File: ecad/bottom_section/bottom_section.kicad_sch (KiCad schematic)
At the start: 5 parts, among them J1 JST PH 3, J3 JST PH 3, J5 Conn_01x08

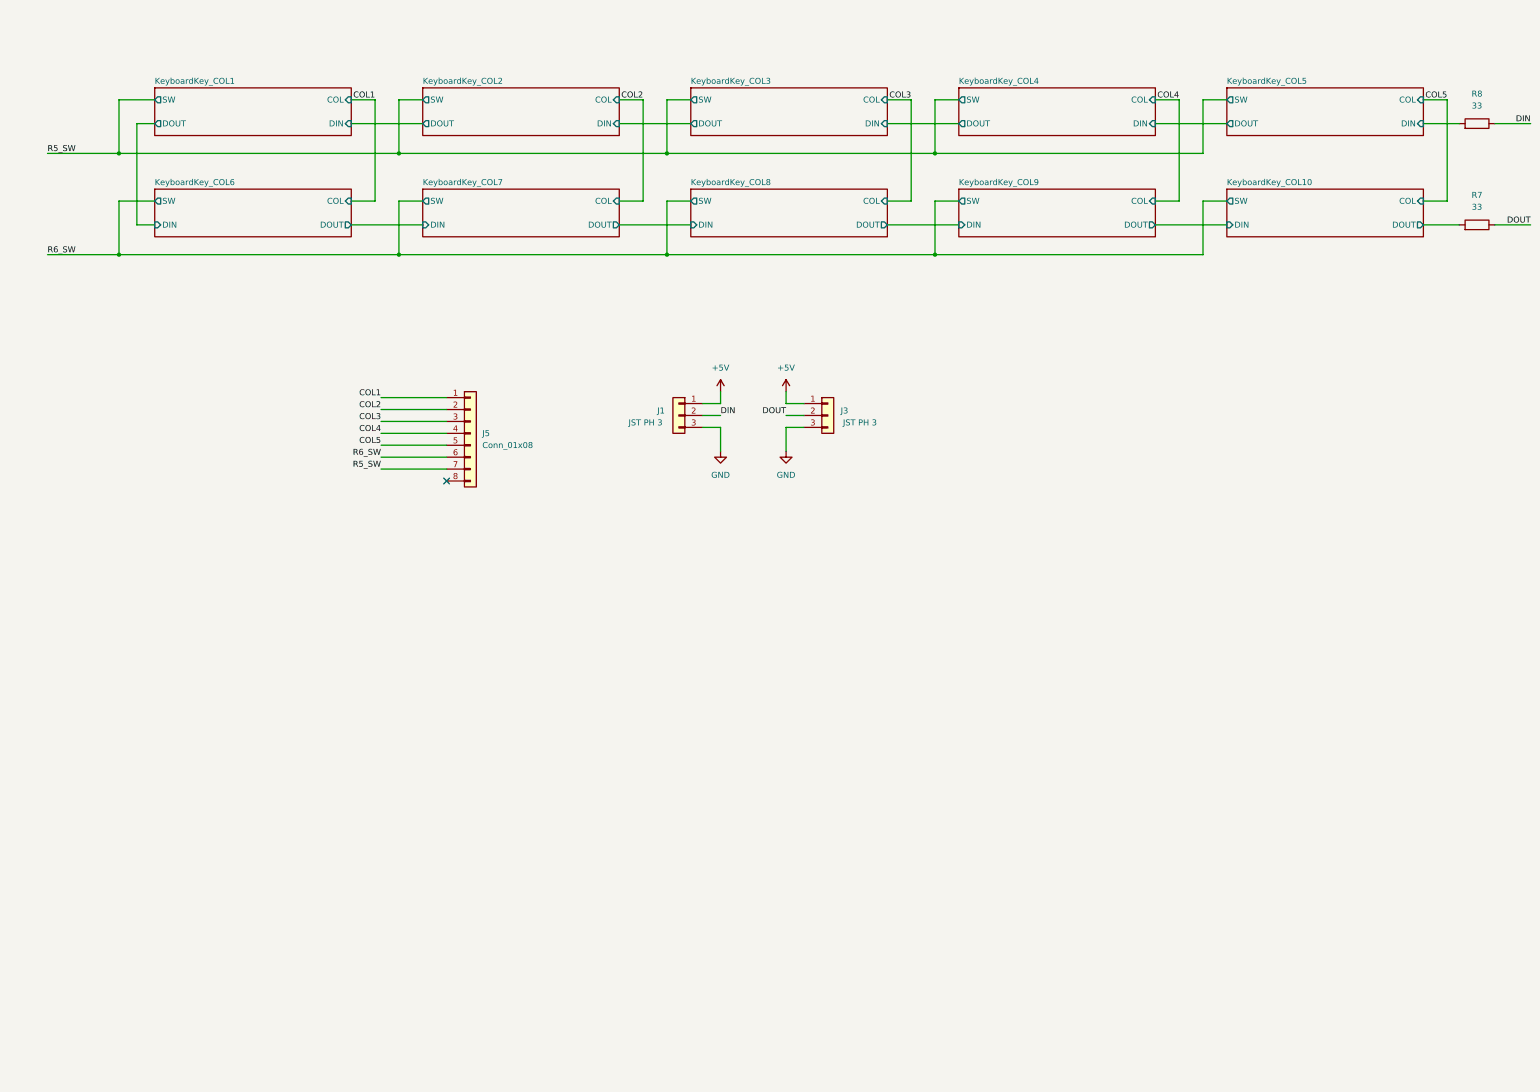
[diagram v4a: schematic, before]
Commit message: Uses LED Matrix controller on all board.
It simplifies so much the design for a small cost.
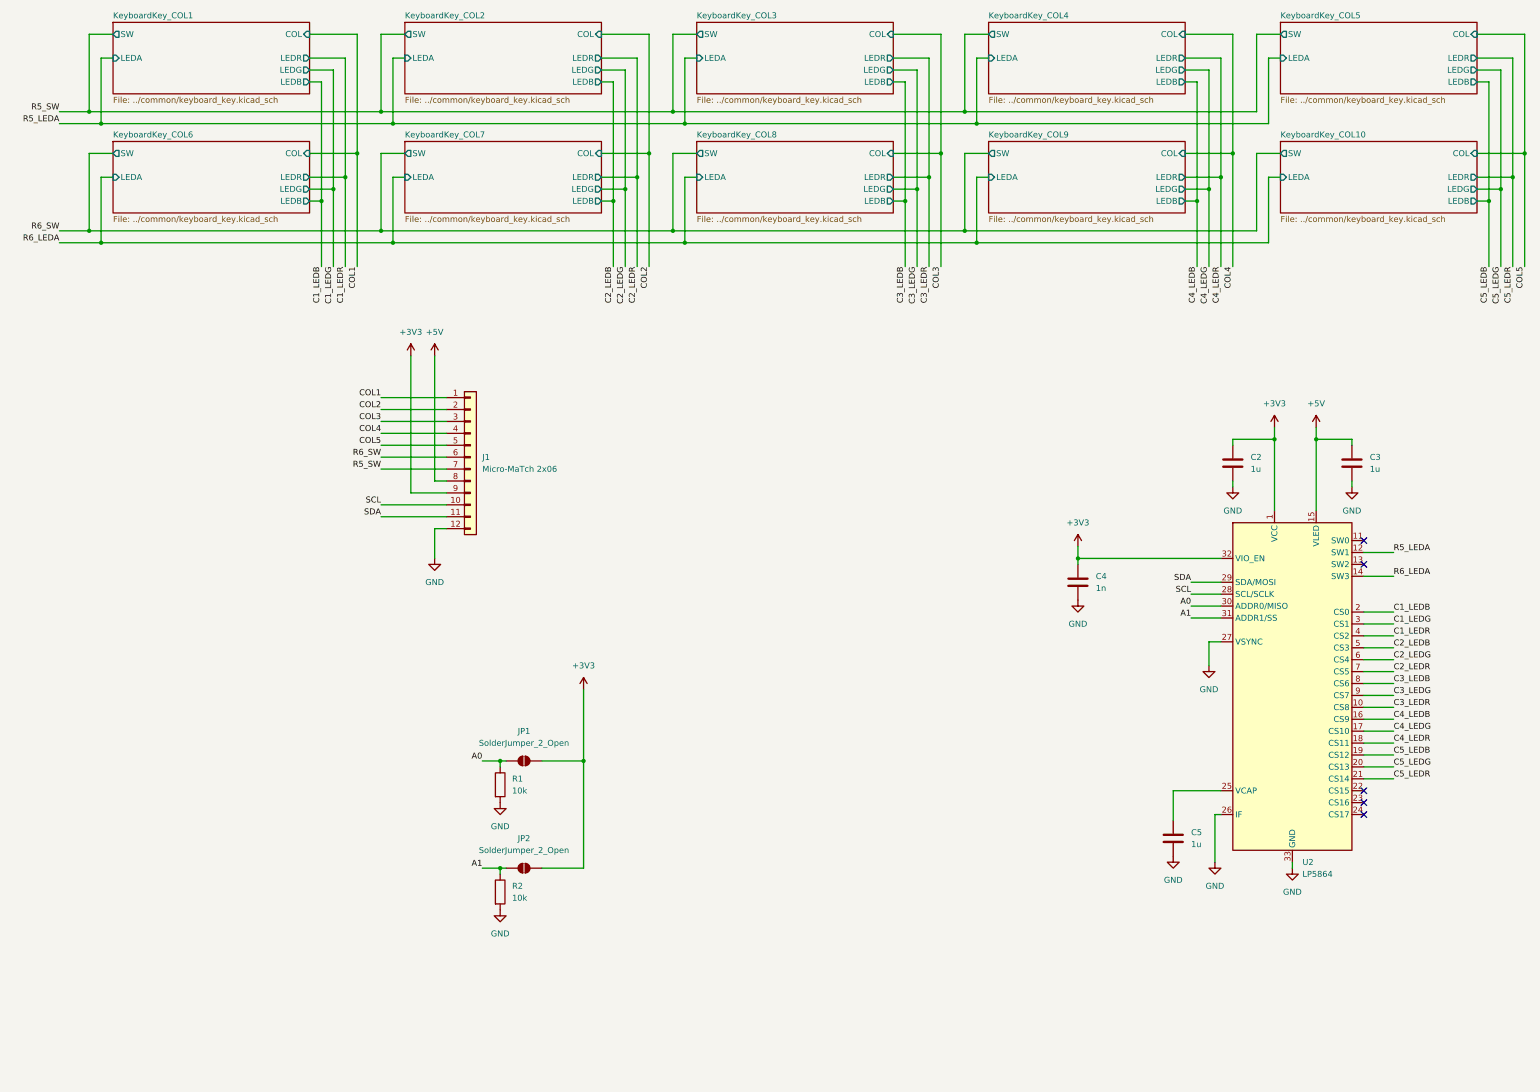
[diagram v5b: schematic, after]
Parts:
- removed J1, J3: JST PH 3, woodpecker:JST_PH_S3B-PH-SM4-TB_1x03-1MP_P2.00mm_Horizontal, symbol Connector_Generic:Conn_01x03
- removed J5: Conn_01x08, Connector_TE-Connectivity:TE_Micro-MaTch_215079-8_2x04_P1.27mm_Vertical, symbol Connector_Generic:Conn_01x08
- removed R7, R8: 33, Resistor_SMD:R_0603_1608Metric, symbol Device:R
- added C2, C3, C5: 1u, Capacitor_SMD:C_0402_1005Metric, symbol Device:C
- added C4: 1n, Capacitor_SMD:C_0402_1005Metric, symbol Device:C
- added J1: Micro-MaTch 2x06, Connector_TE-Connectivity:TE_Micro-MaTch_1-215079-2_2x06_P1.27mm_Vertical, symbol Connector_Generic:Conn_01x12
- added JP1, JP2: SolderJumper_2_Open, Jumper:SolderJumper-2_P1.3mm_Open_TrianglePad1.0x1.5mm, symbol Jumper:SolderJumper_2_Open
- added R1, R2: 10k, Resistor_SMD:R_0603_1608Metric, symbol Device:R
- added U2: LP5864, woodpecker:Texas_LP586X_VQFN-32-1EP_4x4mm_P0.4mm_EP2.8x2.8mm_ThermalVias, symbol woodpecker:LP5864
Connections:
- net +5V: now also C3.1, J1.8 (Pin_8), U2.15 (VLED)
- net COL1: now also J1.1 (Pin_1)
- net COL2: now also J1.2 (Pin_2)
- net COL3: now also J1.3 (Pin_3)
- net COL4: now also J1.4 (Pin_4)
- net COL5: now also J1.5 (Pin_5)
- net GND: now also C2.2, C3.2, C4.2, C5.2, J1.12 (Pin_12), R1.2, R2.2, U2.26 (IF), U2.27 (VSYNC), U2.33 (GND)
- net R5_SW: now also J1.7 (Pin_7)
- net R6_SW: now also J1.6 (Pin_6)
- new net: C5.1, U2.25 (VCAP)
- new net +3V3: C2.1, C4.1, J1.9 (Pin_9), JP1.2 (B), JP2.2 (B), U2.1 (VCC), U2.32 (VIO_EN)
- new net A0: JP1.1 (A), R1.1, U2.30 (ADDR0/MISO)
- new net A1: JP2.1 (A), R2.1, U2.31 (ADDR1/SS)
- new net C1_LEDB: U2.2 (CS0)
- new net C1_LEDG: U2.3 (CS1)
- new net C1_LEDR: U2.4 (CS2)
- new net C2_LEDB: U2.5 (CS3)
- new net C2_LEDG: U2.6 (CS4)
- new net C2_LEDR: U2.7 (CS5)
- new net C3_LEDB: U2.8 (CS6)
- new net C3_LEDG: U2.9 (CS7)
- new net C3_LEDR: U2.10 (CS8)
- new net C4_LEDB: U2.16 (CS9)
- new net C4_LEDG: U2.17 (CS10)
- new net C4_LEDR: U2.18 (CS11)
- new net C5_LEDB: U2.19 (CS12)
- new net C5_LEDG: U2.20 (CS13)
- new net C5_LEDR: U2.21 (CS14)
- new net R5_LEDA: U2.12 (SW1)
- new net R6_LEDA: U2.14 (SW3)
- new net SCL: J1.10 (Pin_10), U2.28 (SCL/SCLK)
- new net SDA: J1.11 (Pin_11), U2.29 (SDA/MOSI)
- no-connect marks 1 -> 5
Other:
- sheet KeyboardKey_COL1 ports: added LEDA, LEDB, LEDG, LEDR; removed DIN, DOUT
- sheet KeyboardKey_COL10 ports: added LEDA, LEDB, LEDG, LEDR; removed DIN, DOUT
- sheet KeyboardKey_COL2 ports: added LEDA, LEDB, LEDG, LEDR; removed DIN, DOUT
- sheet KeyboardKey_COL3 ports: added LEDA, LEDB, LEDG, LEDR; removed DIN, DOUT
- sheet KeyboardKey_COL4 ports: added LEDA, LEDB, LEDG, LEDR; removed DIN, DOUT
- sheet KeyboardKey_COL5 ports: added LEDA, LEDB, LEDG, LEDR; removed DIN, DOUT
- sheet KeyboardKey_COL6 ports: added LEDA, LEDB, LEDG, LEDR; removed DIN, DOUT
- sheet KeyboardKey_COL7 ports: added LEDA, LEDB, LEDG, LEDR; removed DIN, DOUT
- sheet KeyboardKey_COL8 ports: added LEDA, LEDB, LEDG, LEDR; removed DIN, DOUT
- sheet KeyboardKey_COL9 ports: added LEDA, LEDB, LEDG, LEDR; removed DIN, DOUT

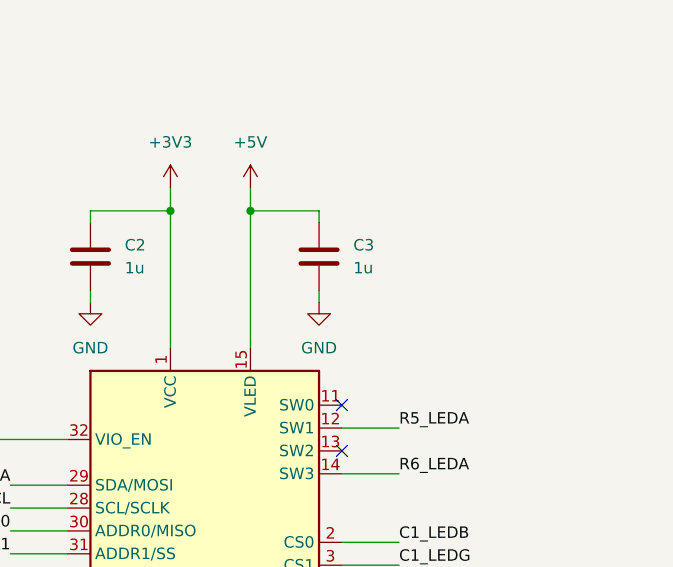
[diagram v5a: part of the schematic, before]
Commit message: Updated Controller for I2C controlled LED Matrices
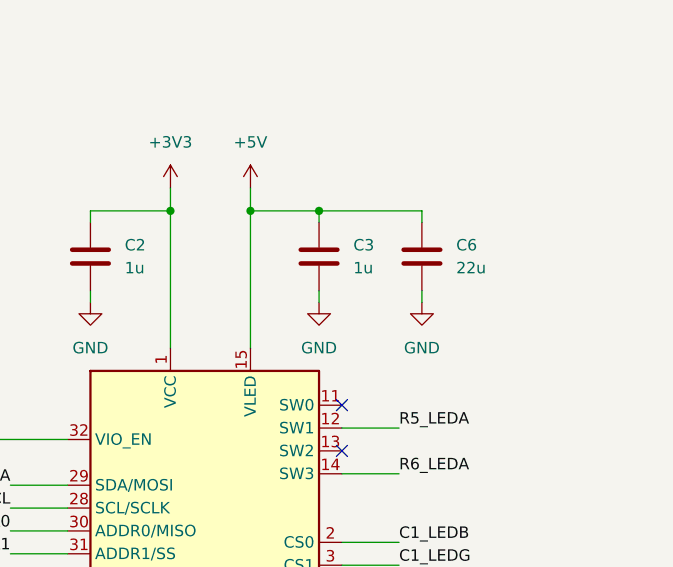
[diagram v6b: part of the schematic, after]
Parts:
- added C6: 22u, Capacitor_SMD:C_0805_2012Metric, symbol Device:C
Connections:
- net +5V: now also C6.1
- net GND: now also C6.2
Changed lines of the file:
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@@
 	)
 	(junction
+		(at 322.58 113.03)
+		(diameter 0)
+		(color 0 0 0 0)
+	)
+	(junction
 		(at 297.18 52.07)
 		(diameter 0)
@@
 	(wire
 		(pts
+			(xy 334.01 121.92) (xy 334.01 123.19)
+		)
+		(stroke
+			(width 0)
+			(type default)
+		)
+	)
+	(wire
+		(pts
 			(xy 224.79 62.23) (xy 227.33 62.23)
 		)
@@
 	(wire
 		(pts
+			(xy 322.58 113.03) (xy 334.01 113.03)
+		)
+		(stroke
+			(width 0)
+			(type default)
+		)
+	)
+	(wire
+		(pts
 			(xy 302.26 52.07) (xy 302.26 68.58)
 		)
@@
 	(wire
 		(pts
+			(xy 334.01 113.03) (xy 334.01 114.3)
+		)
+		(stroke
+			(width 0)
+			(type default)
+		)
+	)
+	(wire
+		(pts
 			(xy 297.18 52.07) (xy 297.18 76.2)
 		)
@@
 	)
 	(symbol
+		(lib_id "Device:C")
+		(at 334.01 118.11 0)
+		(unit 1)
+		(exclude_from_sim no)
+		(in_bom yes)
+		(on_board yes)
+		(dnp no)
+		(fields_autoplaced yes)
+		(property "Reference" "C6"
+			(at 337.82 116.8399 0)
+			(effects
+				(font
+					(size 1.27 1.27)
+				)
+				(justify left)
+			)
+		)
+		(property "Value" "22u"
+			(at 337.82 119.3799 0)
+			(effects
+				(font
+					(size 1.27 1.27)
+				)
+				(justify left)
+			)
+		)
+		(property "Footprint" "Capacitor_SMD:C_0805_2012Metric"
+			(at 334.9752 121.92 0)
+			(effects
+				(font
+					(size 1.27 1.27)
+				)
+				(hide yes)
+			)
+		)
+		(property "Datasheet" "~"
+			(at 334.01 118.11 0)
+			(effects
+				(font
+					(size 1.27 1.27)
+				)
+				(hide yes)
+			)
+		)
+		(property "Description" "Unpolarized capacitor"
+			(at 334.01 118.11 0)
+			(effects
+				(font
+					(size 1.27 1.27)
+				)
+				(hide yes)
+			)
+		)
+		(property "Manufacturer" ""
+			(at 334.01 118.11 0)
+			(effects
+				(font
+					(size 1.27 1.27)
+				)
+				(hide yes)
+			)
+		)
+		(pin "2"
+		)
+		(pin "1"
+		)
+		(instances
+			(project "bottom_section"
+				(path "/e5586514-98d8-4785-a096-88fc3a51b1f3"
+					(reference "C6")
+					(unit 1)
+				)
+			)
+		)
+	)
+	(symbol
 		(lib_id "power:+5V")
 		(at 158.75 166.37 0)
@@
 					(unit 1)
 				)
+			)
+		)
+	)
+	(symbol
+		(lib_id "power:GND")
+		(at 334.01 123.19 0)
+		(unit 1)
+		(exclude_from_sim no)
+		(in_bom yes)
+		(on_board yes)
+		(dnp no)
+		(fields_autoplaced yes)
+		(property "Reference" "#PWR022"
+			(at 334.01 129.54 0)
+			(effects
+				(font
+					(size 1.27 1.27)
+				)
+				(hide yes)
+			)
+		)
+		(property "Value" "GND"
+			(at 334.01 128.27 0)
+			(effects
+				(font
+					(size 1.27 1.27)
+				)
+			)
+		)
+		(property "Footprint" ""
+			(at 334.01 123.19 0)
+			(effects
+				(font
+					(size 1.27 1.27)
+				)
+				(hide yes)
+			)
+		)
+		(property "Datasheet" ""
+			(at 334.01 123.19 0)
+			(effects
+				(font
+					(size 1.27 1.27)
+				)
+				(hide yes)
+			)
+		)
+		(property "Description" "Power symbol creates a global label with name \"GND\" , ground"
+			(at 334.01 123.19 0)
+			(effects
+				(font
+					(size 1.27 1.27)
+				)
+				(hide yes)
+			)
+		)
+		(pin "1"
+		)
+		(instances
+			(project "bottom_section"
+				(path "/e5586514-98d8-4785-a096-88fc3a51b1f3"
+					(reference "#PWR022")
+					(unit 1)
+				)

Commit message: First production run for PCB
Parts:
- C2, C3, C5: MPN (none) -> GCM155C71A105KE38D
- C4: MPN (none) -> KGM05AR71A102KH
- C6: MPN (none) -> GRM21BZ71A226ME15L
- J1: MPN 1-188275-2 -> 1-215079-2
- R1, R2: value 10k -> 33k; MPN (none) -> RC0603FR-0733KL
- U2: MPN LP5864 -> LP5864RSMR
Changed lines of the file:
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@@
+			)
+		)
+		(property "MPN" "GRM21BZ71A226ME15L"
+			(at 334.01 118.11 0)
+			(effects
+				(font
+					(size 1.27 1.27)
+				)
+				(hide yes)
 			)
 		)
@@
 			)
 		)
-		(property "MPN" "1-188275-2"
+		(property "MPN" "1-215079-2"
 			(at 134.62 116.84 0)
 			(effects
@@
 			)
 		)
+		(property "MPN" "GCM155C71A105KE38D"
+			(at 322.58 118.11 0)
+			(effects
+				(font
+					(size 1.27 1.27)
+				)
+				(hide yes)
+			)
+		)
 		(pin "2"
 		)
@@
 		)
 		(property "Manufacturer" ""
+			(at 284.48 198.12 0)
+			(effects
+				(font
+					(size 1.27 1.27)
+				)
+				(hide yes)
+			)
+		)
+		(property "MPN" "GCM155C71A105KE38D"
 			(at 284.48 198.12 0)
 			(effects
@@
 			)
 		)
+		(property "MPN" "KGM05AR71A102KH"
+			(at 264.16 143.51 0)
+			(effects
+				(font
+					(size 1.27 1.27)
+				)
+				(hide yes)
+			)
+		)
 		(pin "2"
 		)
@@
 			)
 		)
-		(property "Value" "10k"
+		(property "Value" "33k"
 			(at 143.51 187.9599 0)
 			(effects
@@
 			)
 		)
+		(property "MPN" "RC0603FR-0733KL"
+			(at 140.97 186.69 0)
+			(effects
+				(font
+					(size 1.27 1.27)
+				)
+				(hide yes)
+			)
+		)
 		(pin "2"
 		)
@@
 			)
 		)
-		(property "Value" "10k"
+		(property "Value" "33k"
 			(at 143.51 210.8199 0)
 			(effects
@@
 			)
 		)
+		(property "MPN" "RC0603FR-0733KL"
+			(at 140.97 209.55 0)
+			(effects
+				(font
+					(size 1.27 1.27)
+				)
+				(hide yes)
+			)
+		)
 		(pin "2"
 		)
@@
 			)
 		)
-		(property "MPN" "LP5864"
+		(property "MPN" "LP5864RSMR"
 			(at 309.88 165.1 0)
 			(effects
@@
 			(at 297.18 118.11 0)
 			(effects
+				(font
+					(size 1.27 1.27)
+				)
+				(hide yes)
+			)
+		)
+		(property "MPN" "GCM155C71A105KE38D"
+			(at 297.18 118.11 0)
+			(effects

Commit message: Outputs new  step files
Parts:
- J1: footprint Connector_TE-Connectivity:TE_Micro-MaTch_1-215079-2_2x06_P1.27mm_Vertical -> woodpecker:TE_Micro-MaTch_1-215079-2_2x06_P1.27mm_Vertical
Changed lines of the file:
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@@
 			)
 		)
-		(property "Footprint" "Connector_TE-Connectivity:TE_Micro-MaTch_1-215079-2_2x06_P1.27mm_Vertical"
+		(property "Footprint" "woodpecker:TE_Micro-MaTch_1-215079-2_2x06_P1.27mm_Vertical"
 			(at 134.62 116.84 0)
 			(effects
